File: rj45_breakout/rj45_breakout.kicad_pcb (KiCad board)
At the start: 2 copper layers, 64.1 x 80.6 mm, 17 parts, among them J10 Conn_01x08, J6 RJ45_Shielded, J9 Conn_02x04_Odd_Even

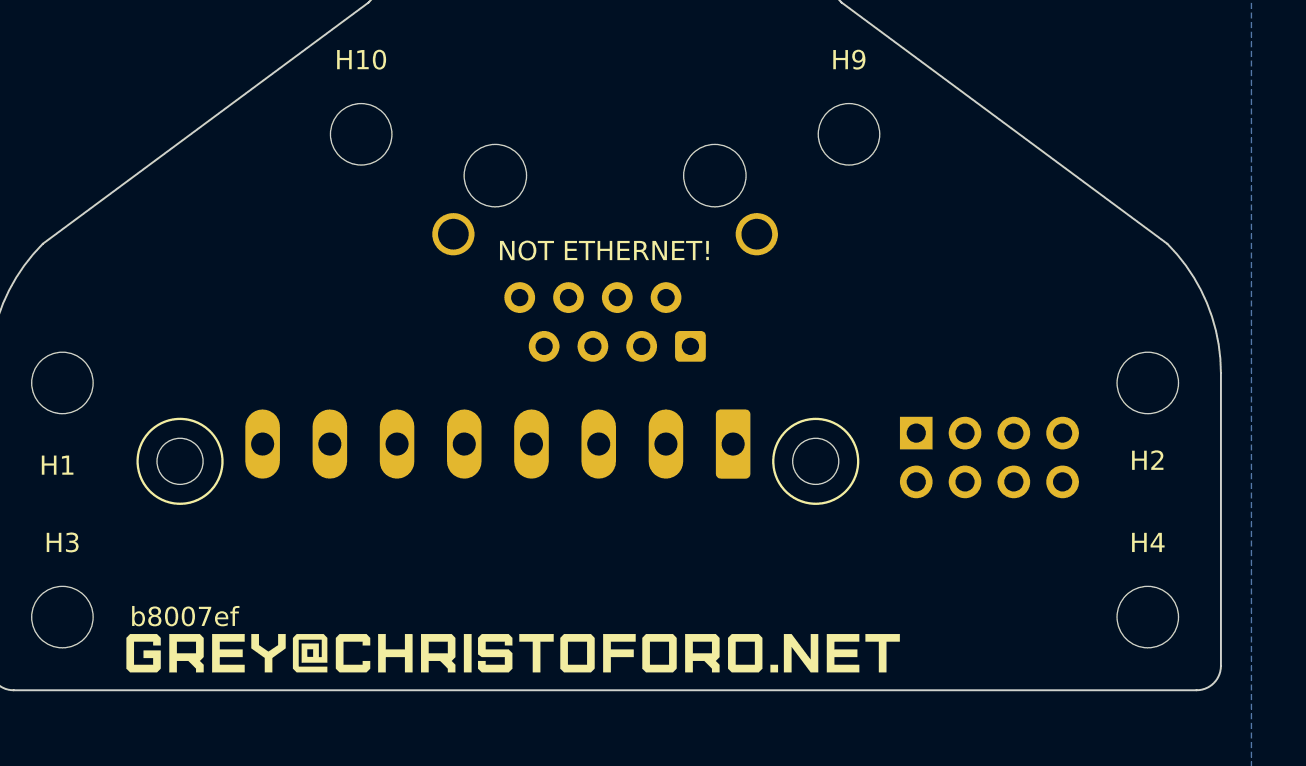
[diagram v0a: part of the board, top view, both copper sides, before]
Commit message: add some missing copper
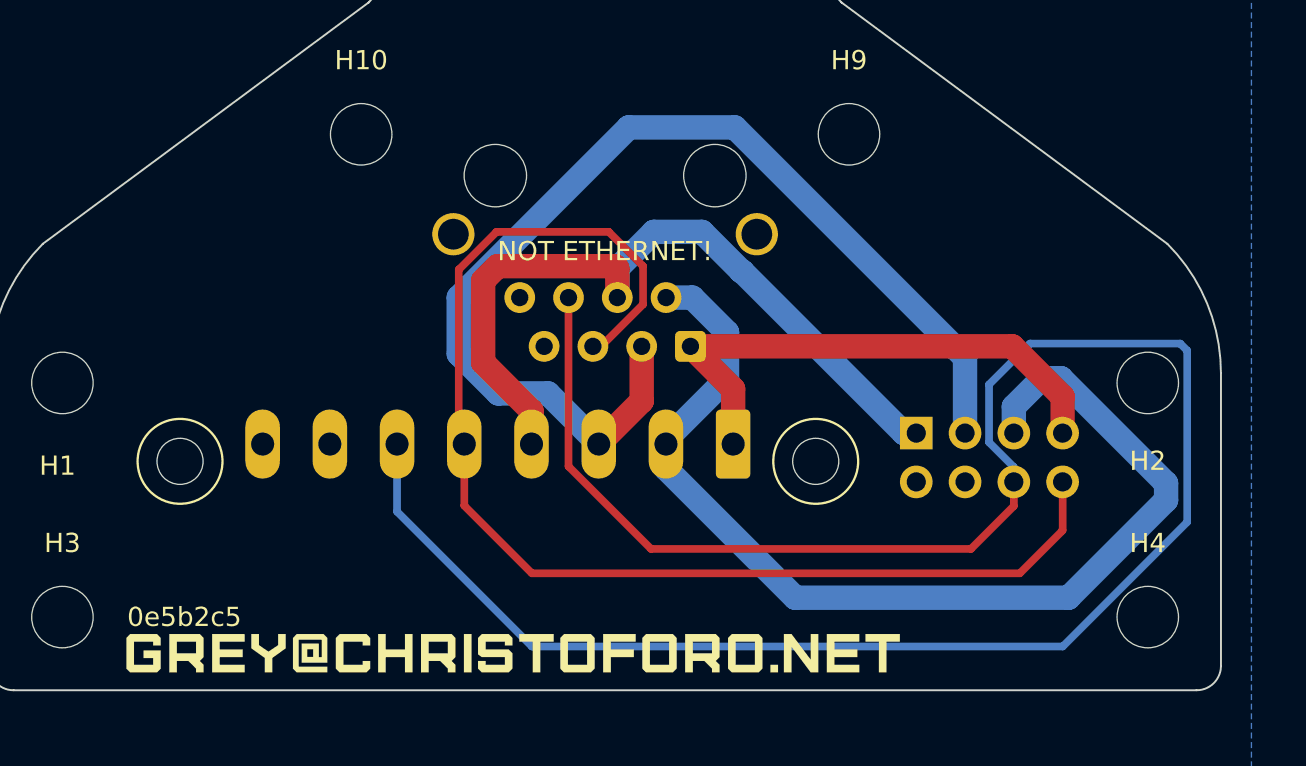
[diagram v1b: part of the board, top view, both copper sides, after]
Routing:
- net /GUARD: track 0.00 -> 112.1 mm
- net /GUARD_SENSE: track 0.00 -> 65.1 mm
- net /LO_SENSE: track 0.00 -> 57.1 mm
- net /HI_SENSE: track 0.00 -> 56.3 mm
- net /LO_FORCE: track 0.00 -> 40.6 mm
- net /HI_FORCE: track 0.00 -> 28.4 mm
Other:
- board text added: "0e5b2c5"
- board text removed: "b8007ef"
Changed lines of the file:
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@@
   (gr_arc (start 82.2325 45.085001) (mid 82.957547 41.439942) (end 85.022308 38.34981)
     (stroke (width 0.1) (type default)) (layer "Edge.Cuts"))
-  (gr_text "b8007ef" (at 92.3925 57.785) (layer "B.SilkS")
+  (gr_text "0e5b2c5" (at 92.3925 57.785) (layer "B.SilkS")
     (effects (font (size 1 1) (thickness 0.15)) (justify mirror))
   )
@@
     (effects (font (size 1 1) (thickness 0.15)))
   )
-  (gr_text "b8007ef" (at 92.3925 57.785) (layer "F.SilkS")
+  (gr_text "0e5b2c5" (at 92.3925 57.785) (layer "F.SilkS")
     (effects (font (size 1 1) (thickness 0.15)))
   )
+  (segment (start 124.1985 56.776) (end 138.43 56.776) (width 1.27) (layer "B.Cu") (net 1))
+  (segment (start 137.064 45.346) (end 135.5825 46.8275) (width 1.27) (layer "B.Cu") (net 1))
+  (segment (start 143.51 51.696) (end 143.51 50.817775) (width 1.27) (layer "B.Cu") (net 1))
+  (segment (start 138.038225 45.346) (end 137.064 45.346) (width 1.27) (layer "B.Cu") (net 1))
+  (segment (start 138.43 56.776) (end 143.51 51.696) (width 1.27) (layer "B.Cu") (net 1))
+  (segment (start 143.51 50.817775) (end 138.038225 45.346) (width 1.27) (layer "B.Cu") (net 1))
+  (segment (start 117.4675 50.045) (end 124.1985 56.776) (width 1.27) (layer "B.Cu") (net 1))
+  (segment (start 120.65 42.957407) (end 120.65 45.358078) (width 1.27) (layer "B.Cu") (net 1))
+  (segment (start 117.4675 48.775) (end 117.4675 50.045) (width 1.27) (layer "B.Cu") (net 1))
+  (segment (start 120.65 45.358078) (end 117.4675 48.540578) (width 1.27) (layer "B.Cu") (net 1))
+  (segment (start 118.840593 41.148) (end 120.65 42.957407) (width 1.27) (layer "B.Cu") (net 1))
+  (segment (start 135.5825 46.8275) (end 135.5825 48.205) (width 1.27) (layer "B.Cu") (net 1))
+  (segment (start 117.4675 48.540578) (end 117.4675 48.775) (width 1.27) (layer "B.Cu") (net 1))
+  (segment (start 117.475 41.148) (end 118.840593 41.148) (width 1.27) (layer "B.Cu") (net 1))
+  (segment (start 116.205 46.5375) (end 113.9675 48.775) (width 1.27) (layer "F.Cu") (net 2))
+  (segment (start 116.205 43.688) (end 116.205 46.5375) (width 1.27) (layer "F.Cu") (net 2))
+  (segment (start 111.3325 46.14) (end 113.9675 48.775) (width 1.27) (layer "B.Cu") (net 2))
+  (segment (start 121.054676 32.288) (end 115.53038 32.288) (width 1.27) (layer "B.Cu") (net 2))
+  (segment (start 108.744 46.14) (end 111.3325 46.14) (width 1.27) (layer "B.Cu") (net 2))
+  (segment (start 106.68 44.076) (end 108.744 46.14) (width 1.27) (layer "B.Cu") (net 2))
+  (segment (start 133.0425 48.205) (end 133.0425 44.275824) (width 1.27) (layer "B.Cu") (net 2))
+  (segment (start 115.53038 32.288) (end 106.68 41.13838) (width 1.27) (layer "B.Cu") (net 2))
+  (segment (start 133.0425 44.275824) (end 121.054676 32.288) (width 1.27) (layer "B.Cu") (net 2))
+  (segment (start 106.68 41.13838) (end 106.68 44.076) (width 1.27) (layer "B.Cu") (net 2))
+  (segment (start 135.502 43.688) (end 118.745 43.688) (width 1.27) (layer "F.Cu") (net 3))
+  (segment (start 120.9675 48.775) (end 120.9675 45.9105) (width 1.27) (layer "F.Cu") (net 3))
+  (segment (start 138.1225 46.3085) (end 135.502 43.688) (width 1.27) (layer "F.Cu") (net 3))
+  (segment (start 138.1225 48.205) (end 138.1225 46.3085) (width 1.27) (layer "F.Cu") (net 3))
+  (segment (start 120.9675 45.9105) (end 118.745 43.688) (width 1.27) (layer "F.Cu") (net 3))
   (segment (start 118.745 43.688) (end 118.745 43.688) (width 0.25) (layer "F.Cu") (net 3))
+  (segment (start 114.935 39.631) (end 114.817 39.513) (width 1.27) (layer "F.Cu") (net 4))
+  (segment (start 114.817 39.513) (end 108.703 39.513) (width 1.27) (layer "F.Cu") (net 4))
+  (segment (start 107.95 44.53175) (end 110.4675 47.04925) (width 1.27) (layer "F.Cu") (net 4))
+  (segment (start 107.95 40.266) (end 107.95 44.53175) (width 1.27) (layer "F.Cu") (net 4))
+  (segment (start 110.4675 47.04925) (end 110.4675 48.775) (width 1.27) (layer "F.Cu") (net 4))
+  (segment (start 114.935 41.148) (end 114.935 39.631) (width 1.27) (layer "F.Cu") (net 4))
+  (segment (start 108.703 39.513) (end 107.95 40.266) (width 1.27) (layer "F.Cu") (net 4))
+  (segment (start 114.935 41.148) (end 114.935 39.631) (width 1.27) (layer "B.Cu") (net 4))
+  (segment (start 121.437 39.783) (end 129.859 48.205) (width 1.27) (layer "B.Cu") (net 4))
+  (segment (start 114.935 39.631) (end 116.84 37.726) (width 1.27) (layer "B.Cu") (net 4))
+  (segment (start 121.398496 39.783) (end 121.437 39.783) (width 1.27) (layer "B.Cu") (net 4))
+  (segment (start 129.859 48.205) (end 130.5025 48.205) (width 1.27) (layer "B.Cu") (net 4))
+  (segment (start 119.341496 37.726) (end 121.398496 39.783) (width 1.27) (layer "B.Cu") (net 4))
+  (segment (start 116.84 37.726) (end 119.341496 37.726) (width 1.27) (layer "B.Cu") (net 4))
+  (segment (start 114.493712 37.726) (end 108.643321 37.726) (width 0.4) (layer "F.Cu") (net 6))
+  (segment (start 110.49 55.506) (end 135.89 55.506) (width 0.4) (layer "F.Cu") (net 6))
+  (segment (start 116.275 41.505057) (end 116.275 39.507288) (width 0.4) (layer "F.Cu") (net 6))
+  (segment (start 108.643321 37.726) (end 106.68 39.689321) (width 0.4) (layer "F.Cu") (net 6))
+  (segment (start 106.9675 48.775) (end 106.9675 51.9835) (width 0.4) (layer "F.Cu") (net 6))
+  (segment (start 138.1225 53.2735) (end 138.1225 50.745) (width 0.4) (layer "F.Cu") (net 6))
+  (segment (start 106.68 48.4875) (end 106.9675 48.775) (width 0.4) (layer "F.Cu") (net 6))
+  (segment (start 106.9675 51.9835) (end 110.49 55.506) (width 0.4) (layer "F.Cu") (net 6))
+  (segment (start 116.275 39.507288) (end 114.493712 37.726) (width 0.4) (layer "F.Cu") (net 6))
+  (segment (start 106.68 39.689321) (end 106.68 48.4875) (width 0.4) (layer "F.Cu") (net 6))
+  (segment (start 113.665 43.688) (end 114.092057 43.688) (width 0.4) (layer "F.Cu") (net 6))
+  (segment (start 135.89 55.506) (end 138.1225 53.2735) (width 0.4) (layer "F.Cu") (net 6))
+  (segment (start 114.092057 43.688) (end 116.275 41.505057) (width 0.4) (layer "F.Cu") (net 6))
+  (segment (start 112.395 49.940978) (end 116.690022 54.236) (width 0.4) (layer "F.Cu") (net 7))
+  (segment (start 116.690022 54.236) (end 133.35 54.236) (width 0.4) (layer "F.Cu") (net 7))
+  (segment (start 112.395 41.148) (end 112.395 49.940978) (width 0.4) (layer "F.Cu") (net 7))
+  (segment (start 133.35 54.236) (end 135.5825 52.0035) (width 0.4) (layer "F.Cu") (net 7))
+  (segment (start 135.5825 52.0035) (end 135.5825 50.745) (width 0.4) (layer "F.Cu") (net 7))
+  (segment (start 144.247 43.543) (end 136.423 43.543) (width 0.4) (layer "B.Cu") (net 7))
+  (segment (start 144.6075 52.835862) (end 144.6075 43.9035) (width 0.4) (layer "B.Cu") (net 7))
+  (segment (start 103.4675 52.2935) (end 110.49 59.316) (width 0.4) (layer "B.Cu") (net 7))
+  (segment (start 138.127362 59.316) (end 144.6075 52.835862) (width 0.4) (layer "B.Cu") (net 7))
+  (segment (start 134.2925 48.682767) (end 135.5825 49.972767) (width 0.4) (layer "B.Cu") (net 7))
+  (segment (start 103.4675 48.775) (end 103.4675 52.2935) (width 0.4) (layer "B.Cu") (net 7))
+  (segment (start 134.2925 45.6735) (end 134.2925 48.682767) (width 0.4) (layer "B.Cu") (net 7))
+  (segment (start 136.423 43.543) (end 134.2925 45.6735) (width 0.4) (layer "B.Cu") (net 7))
+  (segment (start 135.5825 49.972767) (end 135.5825 50.745) (width 0.4) (layer "B.Cu") (net 7))
+  (segment (start 144.6075 43.9035) (end 144.247 43.543) (width 0.4) (layer "B.Cu") (net 7))
+  (segment (start 110.49 59.316) (end 138.127362 59.316) (width 0.4) (layer "B.Cu") (net 7))
   (zone (net 8) (net_name "/SHIELD") (layer "F.Cu") (hatch edge 0.508)
     (connect_pads (clearance 0.254))

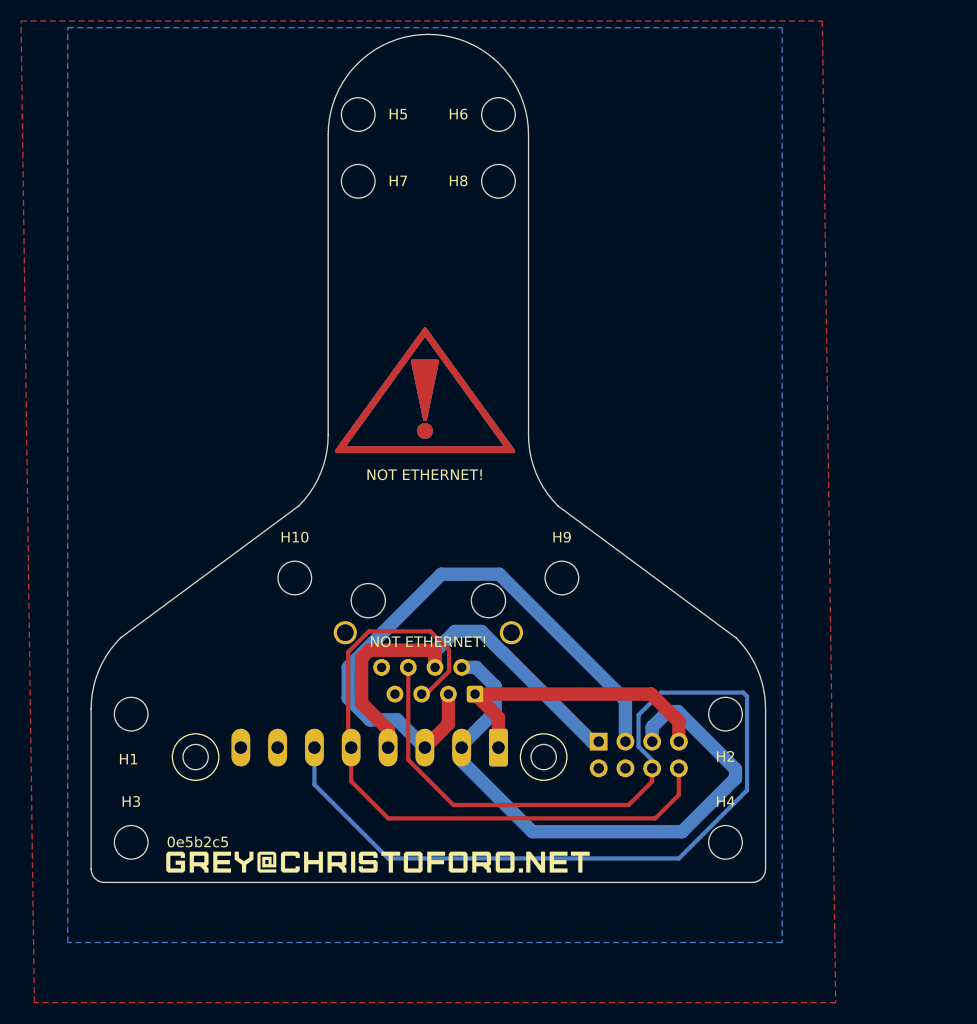
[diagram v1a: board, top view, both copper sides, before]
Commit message: add some missing silkscreen
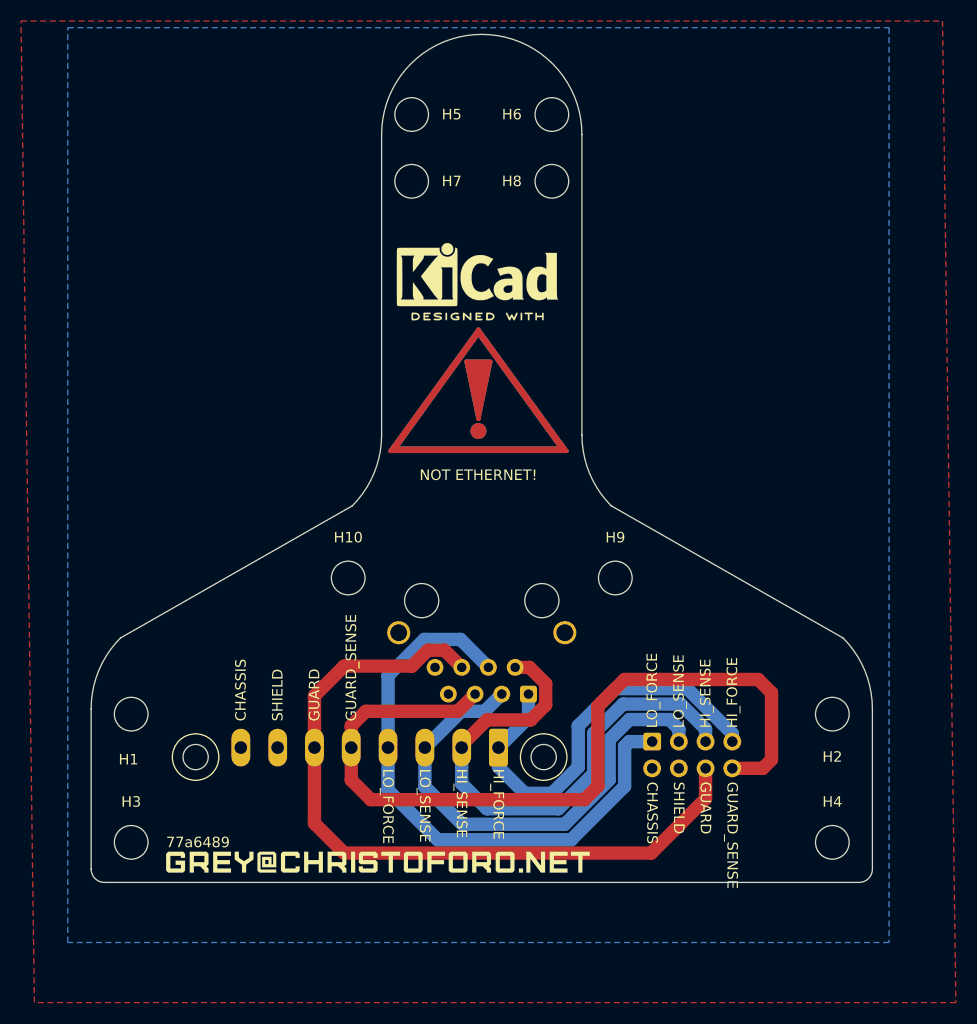
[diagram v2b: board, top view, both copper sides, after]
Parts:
- added REF**: KiCad-Logo2_6mm_SilkScreen, Symbol:KiCad-Logo2_6mm_SilkScreen, F.Cu at (119.0, 3.77)
- added REF**: KiCad-Logo2_6mm_SilkScreen, Symbol:KiCad-Logo2_6mm_SilkScreen, B.Cu at (119.0, 3.77)
- J9: footprint Connector_PinHeader_2.54mm:PinHeader_2x04_P2.54mm_Horizontal -> Connector_IDC:IDC-Header_2x04_P2.54mm_Horizontal
- moved H2 10.2 mm to (152.7, 45.6)
- moved H4 10.2 mm to (152.7, 57.8)
- moved H10 5.08 mm to (106.7, 32.6)
- moved H5 5.08 mm to (112.7, -11.4)
- moved H7 5.08 mm to (112.7, -5.08)
- moved H9 5.08 mm to (132.1, 32.6)
- moved J9 5.08 mm to (135.6, 48.2)
- moved H6 5.08 mm to (126.0, -11.4)
- moved H8 5.08 mm to (126.0, -5.08)
- moved J6 5.08 mm to (119.4, 37.7)
- moved REF** 5.08 mm to (119.1, 15.9) (x2)
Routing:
- net /GUARD: track 112.1 -> 72.0 mm
- net /LO_FORCE: track 40.6 -> 56.1 mm
- net /GUARD_SENSE: track 65.1 -> 79.1 mm
- net /HI_FORCE: track 28.4 -> 40.3 mm
- net /LO_SENSE: track 57.1 -> 46.7 mm
- net /HI_SENSE: track 56.3 -> 51.5 mm
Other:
- board size 64.1 x 80.6 mm -> 74.3 x 80.6 mm
- board text added: "77a6489"
- board text added: "CHASSIS"
- board text added: "GUARD"
- board text added: "GUARD_SENSE"
- board text added: "HI_FORCE"
- board text added: "HI_SENSE"
- board text added: "LO_FORCE"
- board text added: "LO_SENSE"
- board text added: "SHIELD"
- board text removed: "0e5b2c5"

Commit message: update silk
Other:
- board text added: "c5b4c2a"
- board text removed: "77a6489"
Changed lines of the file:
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@@
     (effects (font (size 1 1) (thickness 0.15)) (justify right mirror))
   )
-  (gr_text "77a6489" (at 92.3925 57.785) (layer "B.SilkS")
+  (gr_text "c5b4c2a" (at 92.3925 57.785) (layer "B.SilkS")
     (effects (font (size 1 1) (thickness 0.15)) (justify mirror))
   )
@@
     (effects (font (size 1 1) (thickness 0.15)))
   )
-  (gr_text "77a6489" (at 92.3925 57.785) (layer "F.SilkS")
+  (gr_text "c5b4c2a" (at 92.3925 57.785) (layer "F.SilkS")
     (effects (font (size 1 1) (thickness 0.15)))
   )
